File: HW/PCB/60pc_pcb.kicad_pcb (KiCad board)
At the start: 2 copper layers, 306.5 x 116 mm, 157 parts, among them J1 USB_mini_micro_B, K1 KEYSW, K10 KEYSW, K11 KEYSW, K12 KEYSW, K13 KEYSW, K14 KEYSW, K15 KEYSW, K16 KEYSW, K17 KEYSW, K18 KEYSW, K19 KEYSW, K2 KEYSW, K21 KEYSW, K22 KEYSW, K23 KEYSW, K24 KEYSW, K26 KEYSW, K27 KEYSW, K28 KEYSW, K29 KEYSW, K3 KEYSW, K31 KEYSW, K32 KEYSW, K33 KEYSW, K34 KEYSW, K35 KEYSW, K36 KEYSW, K37 KEYSW, K38 KEYSW, K39 KEYSW, K4 KEYSW, K41 KEYSW, K42 KEYSW, K43 KEYSW, K44 KEYSW, K46 KEYSW, K47 KEYSW, K48 KEYSW, K49 KEYSW, K5 KEYSW, K51 KEYSW, K52 KEYSW, K53 KEYSW, K54 KEYSW, K55 KEYSW, K56 KEYSW, K57 KEYSW, K58 KEYSW, K59 KEYSW, K6 KEYSW, K60 KEYSW, K61 KEYSW, K62 KEYSW, K63 KEYSW, K64 KEYSW, K65 KEYSW, K66 KEYSW, K67 KEYSW, K68 KEYSW, K69 KEYSW, K7 KEYSW, K70 KEYSW, K71 KEYSW, K72 KEYSW, K74 KEYSW, K75 KEYSW, K8 KEYSW, K9 KEYSW, SW1 SW_PUSH, U1 ATMEGA32U4, Y1 Crystal_GND24

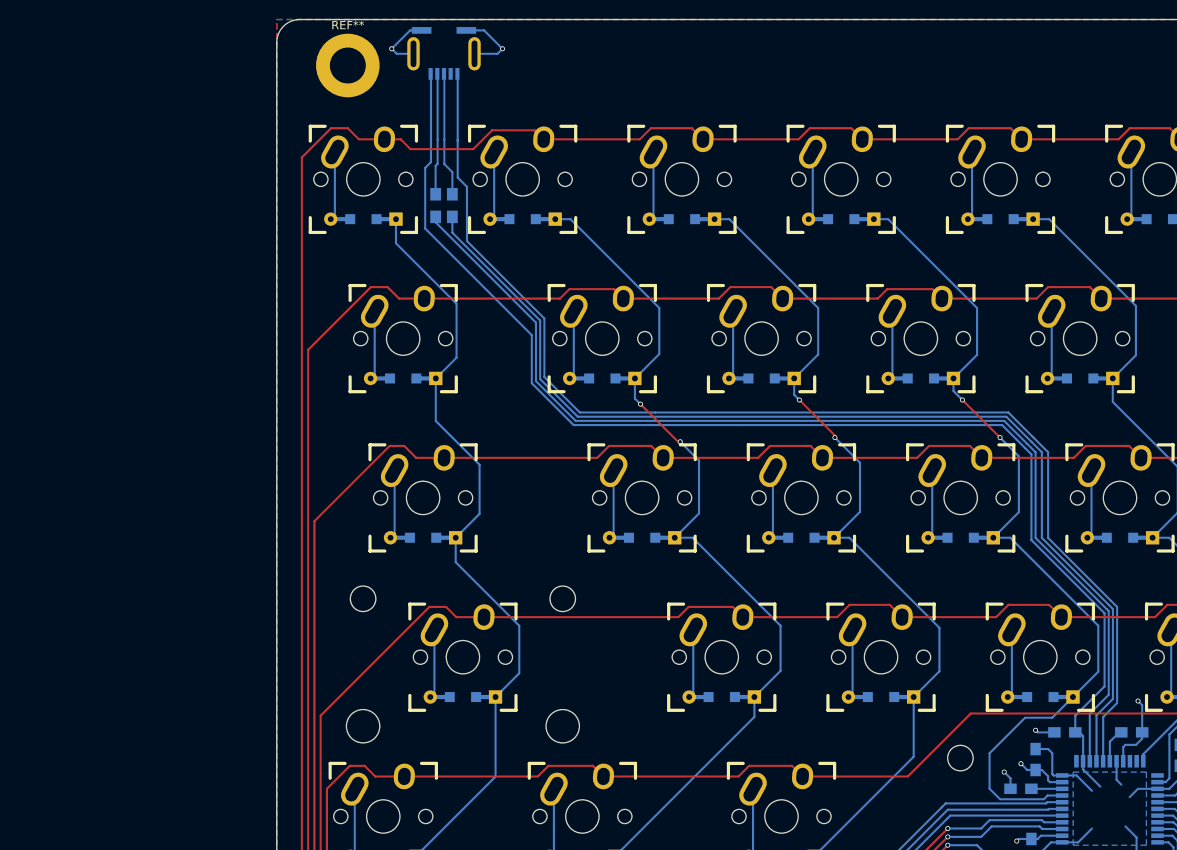
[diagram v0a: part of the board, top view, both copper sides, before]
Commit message: Version 1.1 edits
Smaller form factor.
4x M4 screws to 5x M2 screws.
Screws now placed between switched.
Dufferential routing return path and impedance matching improved.
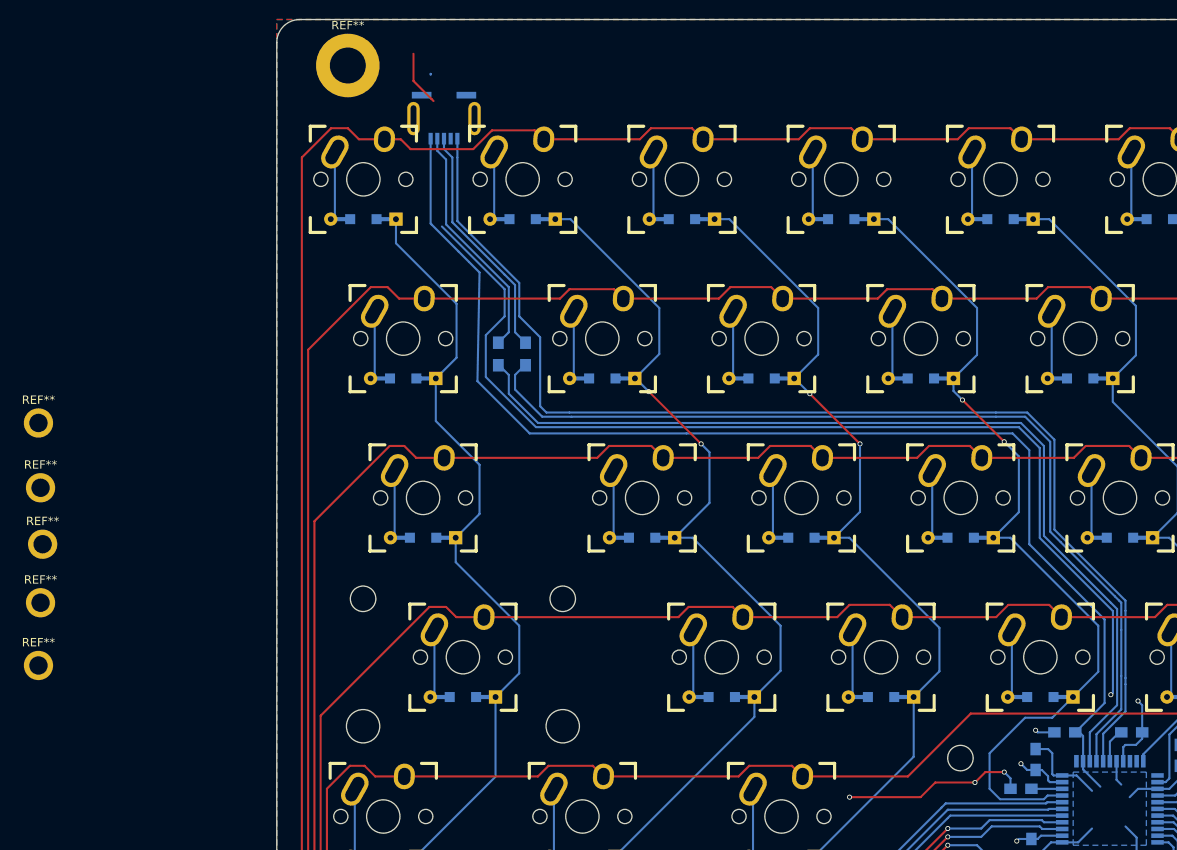
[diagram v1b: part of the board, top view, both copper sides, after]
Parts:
- added REF**: MountingHole_2.2mm_M2_ISO7380_Pad, Mounting_Holes:MountingHole_2.2mm_M2_ISO7380_Pad, F.Cu at (49.2, 72.0)
- added REF**: MountingHole_2.2mm_M2_ISO7380_Pad, Mounting_Holes:MountingHole_2.2mm_M2_ISO7380_Pad, F.Cu at (49.5, 79.8)
- added REF**: MountingHole_2.2mm_M2_ISO7380_Pad, Mounting_Holes:MountingHole_2.2mm_M2_ISO7380_Pad, F.Cu at (49.8, 86.5)
- added REF**: MountingHole_2.2mm_M2_ISO7380_Pad, Mounting_Holes:MountingHole_2.2mm_M2_ISO7380_Pad, F.Cu at (49.5, 93.5)
- added REF**: MountingHole_2.2mm_M2_ISO7380_Pad, Mounting_Holes:MountingHole_2.2mm_M2_ISO7380_Pad, F.Cu at (49.2, 101.0)
- moved R3 19.8 mm to (107.5, 63.8)
- moved R2 19.3 mm to (104.2, 63.8)
- moved J1 7.75 mm to (97.8, 38.0)
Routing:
- net (no net): track 0.00 -> 131.7 mm, vias 1 -> 2
- net Net-(R2-Pad1): track 129.4 -> 113.2 mm
- net Net-(R3-Pad1): track 128.7 -> 113.0 mm
- net Net-(J1-Pad2): track 14.5 -> 28.5 mm
- net Net-(J1-Pad3): track 14.8 -> 28.4 mm
- net VCC: track 246.7 -> 242.5 mm
- net /Col1: track 162.8 -> 163.8 mm
